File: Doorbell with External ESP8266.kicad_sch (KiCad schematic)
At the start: 26 parts, among them J101 Rectifier, J105 Transformer, J106 Button, J107 Chime, K102 Relay, Q102 Q_NMOS_GSD, U101 WeMos_D1_mini, U102 EL817, U104 XC6220B331MR-G

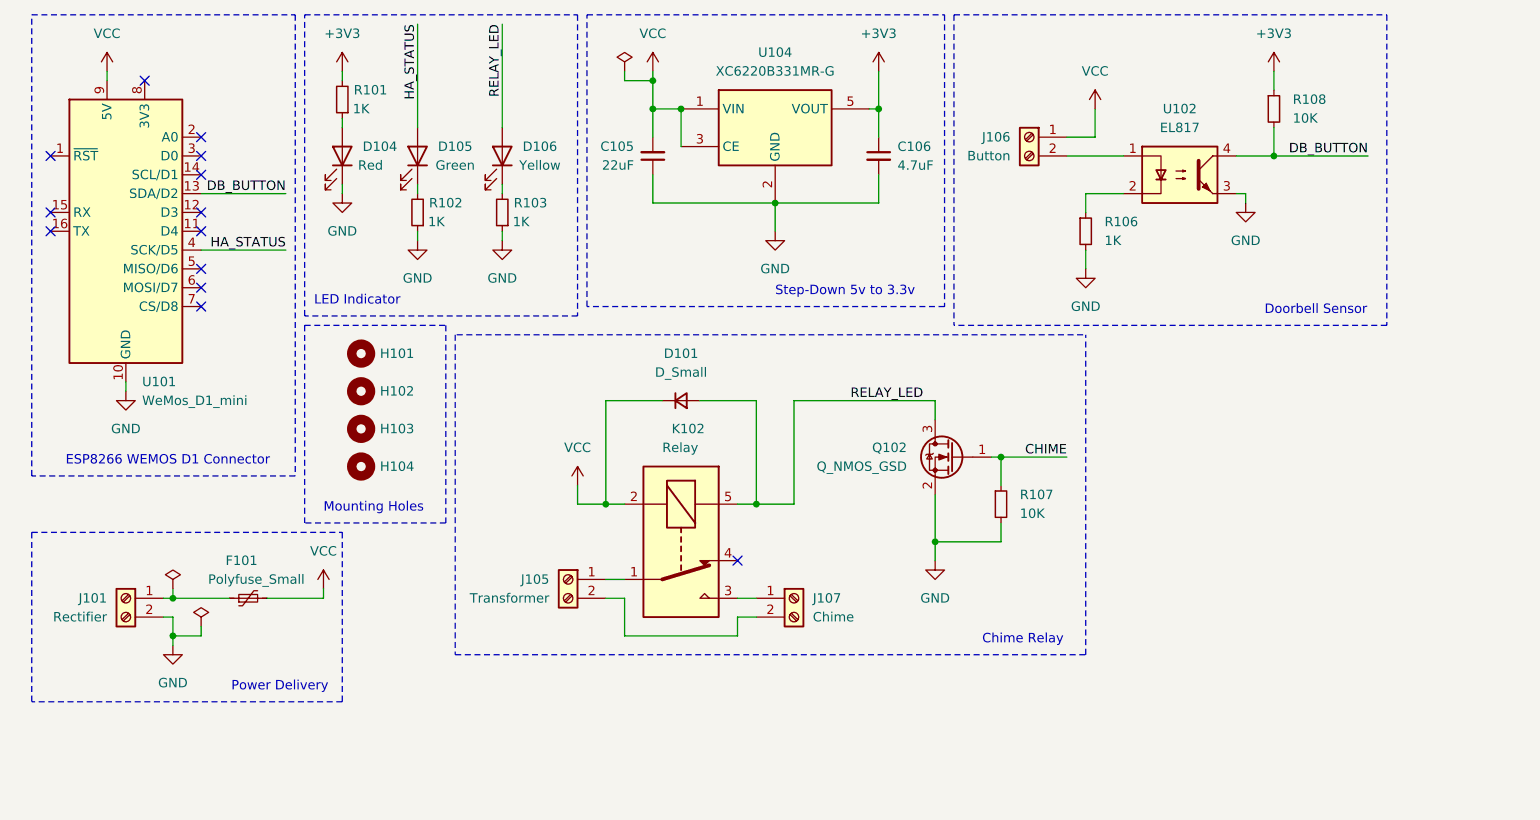
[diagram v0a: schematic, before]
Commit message: Removed CHIME & improved wiring
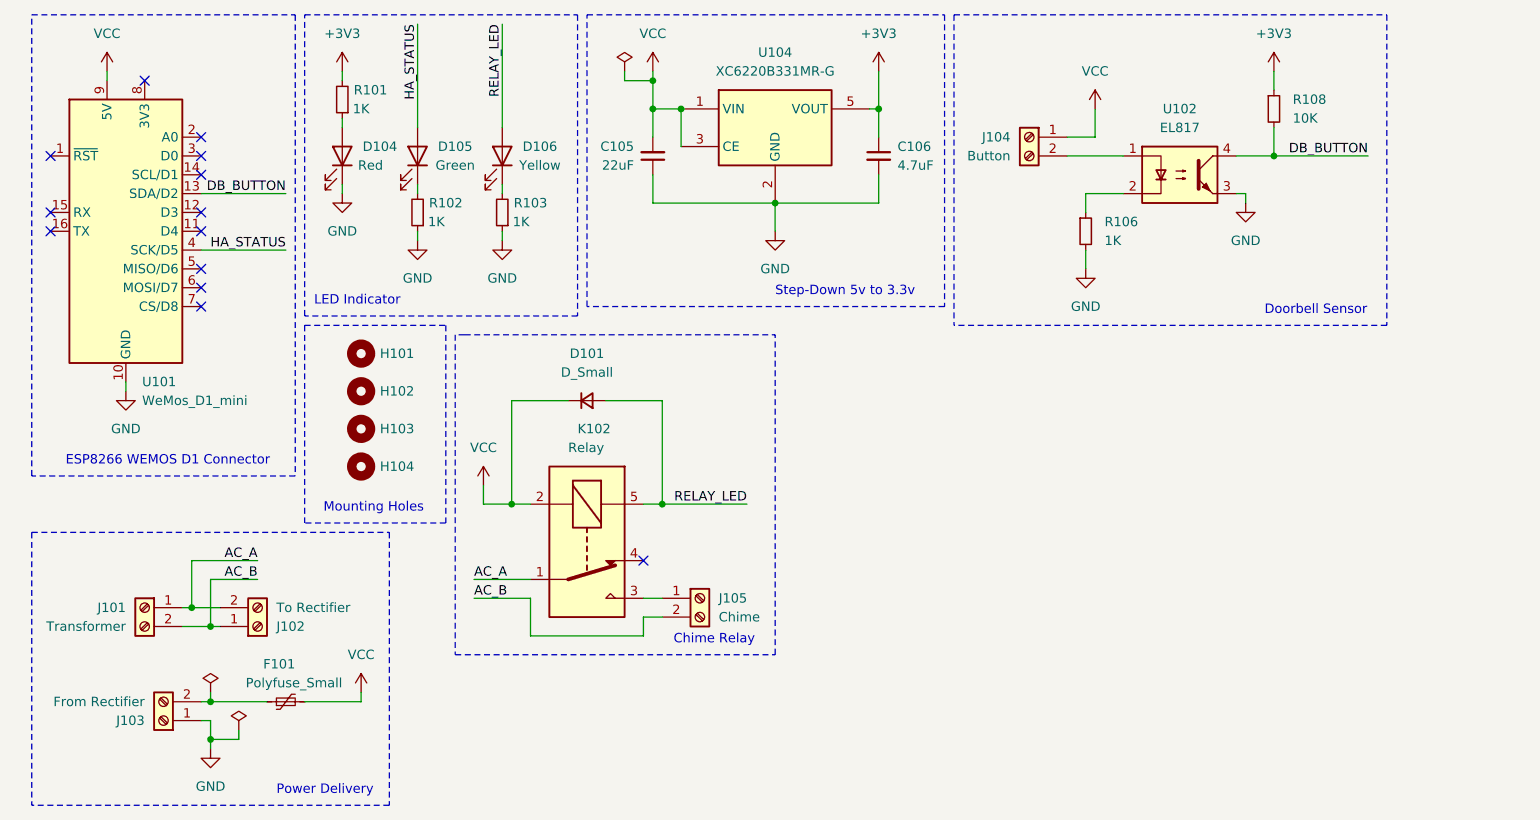
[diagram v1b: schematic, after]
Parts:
- removed J105: Transformer, TerminalBlock_Phoenix:TerminalBlock_Phoenix_MKDS-1,5-2_1x02_P5.00mm_Horizontal, symbol Connector:Screw_Terminal_01x02
- removed Q102: Q_NMOS_GSD, Package_TO_SOT_SMD:SOT-23, symbol Device:Q_NMOS_GSD
- removed R107: 10K, Resistor_SMD:R_0603_1608Metric, symbol Device:R_Small
- added J102: To Rectifier, TerminalBlock_Phoenix:TerminalBlock_Phoenix_MKDS-1,5-2_1x02_P5.00mm_Horizontal, symbol Connector:Screw_Terminal_01x02
- added J103: From Rectifier, TerminalBlock_Phoenix:TerminalBlock_Phoenix_MKDS-1,5-2_1x02_P5.00mm_Horizontal, symbol Connector:Screw_Terminal_01x02
- J101: value Rectifier -> Transformer
- renumbered J106 to J104, J107 to J105
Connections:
- net GND: now also J103.1 (Pin_1); no longer J101.2 (Pin_2)
- net AC_A: now reaches K102.1
- net AC_A: now also J101.1 (Pin_1), J102.2 (Pin_2)
- net AC_B: now reaches J105.2 (Pin_2)
- net AC_B: now also J101.2 (Pin_2), J102.1 (Pin_1)
- net at F101.1: now also J103.2 (Pin_2); no longer J101.1 (Pin_1)
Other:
- moved on the sheet: D101, J105, K102

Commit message: Added ability to control chime from ESP8266
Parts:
- added Q101: Q_NMOS_GSD, Package_TO_SOT_SMD:SOT-23, symbol Device:Q_NMOS_GSD
- added R104: 10K, Resistor_SMD:R_0603_1608Metric, symbol Device:R_Small
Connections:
- net GND: now also Q101.2 (S), R104.2
- net RELAY_LED: now also Q101.3 (D)
- net CHIME: now reaches U101.5 (MISO/D6)
- net CHIME: now also Q101.1 (G), R104.1
- no-connect marks 13 -> 12
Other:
- moved on the sheet: D101, J105, K102

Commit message: Updated schematic & PCB
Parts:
- added D104: White, LED_SMD:LED_0805_2012Metric, symbol Device:LED
- added R104: 1K, Resistor_SMD:R_0603_1608Metric, symbol Device:R_Small
- D101: renamed from D104; footprint LED_SMD:LED_0603_1608Metric -> LED_SMD:LED_0805_2012Metric; LCSC C2286 -> C84256
- D102: renamed from D105; footprint LED_SMD:LED_0603_1608Metric -> LED_SMD:LED_0805_2012Metric; LCSC C72043 -> C2297
- D103: renamed from D106; footprint LED_SMD:LED_0603_1608Metric -> LED_SMD:LED_0805_2012Metric; LCSC C2286 -> C2296
- renumbered C105 to C101, C106 to C102, D101 to D105, J103 to J102, J102 to J103, J105 to J104, J104 to J105, K102 to K101, R104 to R105, R108 to R107, U104 to U102, U102 to U103
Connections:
- net +3V3: now also R103.2, R104.2
- net AC_A: now also J103.1 (Pin_1); no longer J103.2 (Pin_2)
- net AC_B: now also J103.2 (Pin_2); no longer J103.1 (Pin_1)
- net CHIME: now also Q101.2 (S); no longer Q101.1 (G)
- net GND: now also J105.2 (Pin_2), Q101.1 (G); no longer Q101.2 (S), R103.1, R106.2
- net RELAY_LED: now also D104.1 (K); no longer D103.2 (A)
- net VCC: now also U103.1; no longer J105.1 (Pin_1)
- net at U103.2: now also R106.2; no longer R106.1
- net ESP_TX: now reaches U101.16 (TX)
- net ESP_TX: now also D103.1 (K)
- new net: D104.2 (A), R104.1
- new net: D103.2 (A), R103.1
- new net: J105.1 (Pin_1), R106.1
- no-connect marks 12 -> 11
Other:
- moved on the sheet: C101, C102, D101, D102, D103, D105, H101, H102, H103, H104, J103, J104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

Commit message: Moved power to different level & made JLCPCB order
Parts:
- removed C101: 22uF, Capacitor_SMD:C_0603_1608Metric, symbol Device:C_Small
- removed C102: 4.7uF, Capacitor_SMD:C_0603_1608Metric, symbol Device:C_Small
- removed U102: XC6220B331MR-G, Package_TO_SOT_SMD:SOT-23-5, symbol Regulator_Linear:XC6220B331MR
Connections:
- net +3V3: now also U101.8 (3V3)
- no-connect marks 11 -> 10
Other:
- note removed: "Step-Down 5v to 3.3v"
- moved on the sheet: J105, R106, R107, U103

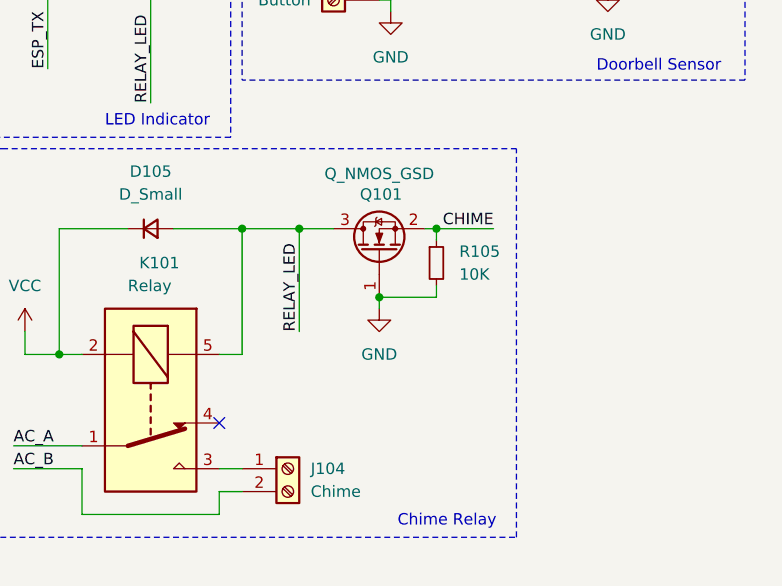
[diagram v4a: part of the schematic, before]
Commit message: Fixed MOSFET for relay & moved some parts around to make it better
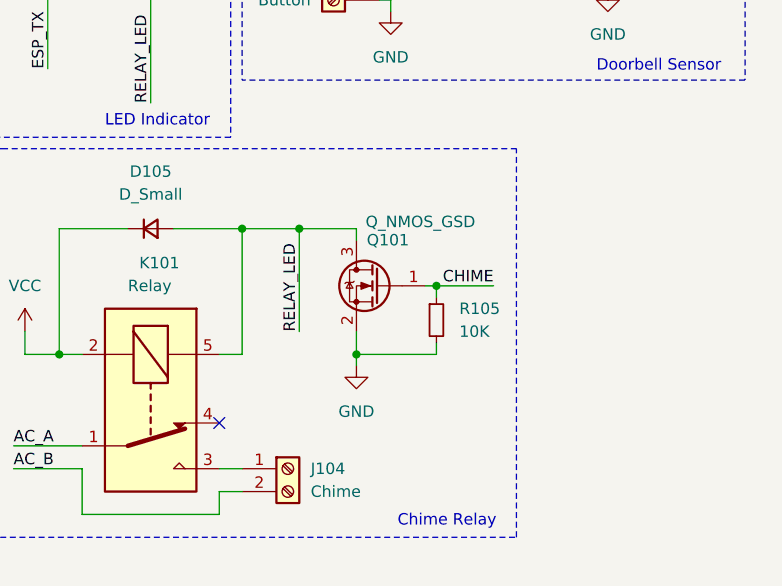
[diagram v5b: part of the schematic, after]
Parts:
- U103: footprint Package_DIP:DIP-4_W7.62mm_SMDSocket_SmallPads -> footprints:EL817S1(C)(TU)-F
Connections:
- net CHIME: now also Q101.1 (G); no longer Q101.2 (S)
- net GND: now also Q101.2 (S); no longer Q101.1 (G)
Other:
- moved on the sheet: Q101, R105
